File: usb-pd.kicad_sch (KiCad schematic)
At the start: 66 parts, among them J3 USB-C_GCT_USB4105-GF-A, Q4 BSS138-7-F, Q6 SQS401EN-T1_BE3, Q8 BSS138-7-F, Q9 BSS138-7-F, U5 CYPD3177-24LQXQ, U9 SIC477ED-T1-GE3

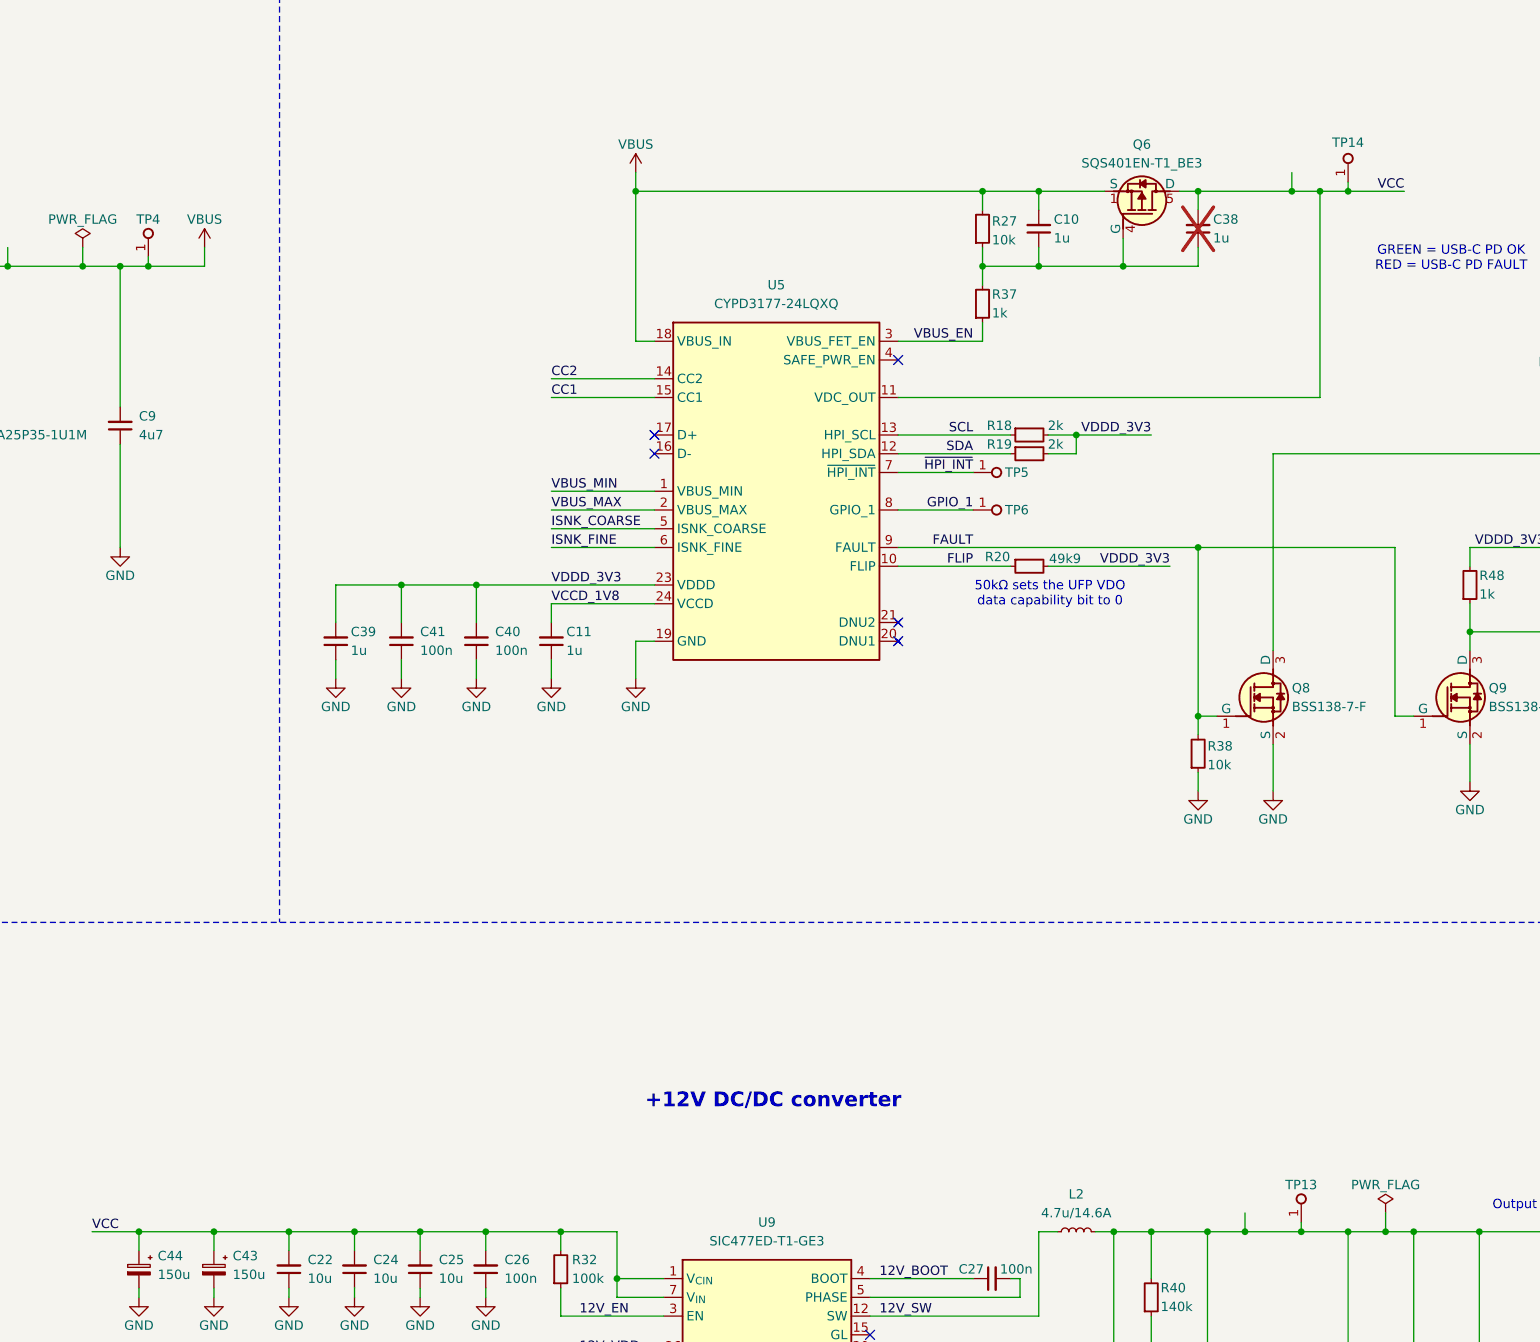
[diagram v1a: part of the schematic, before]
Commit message: [#79790] Added fiducials and double sided test points
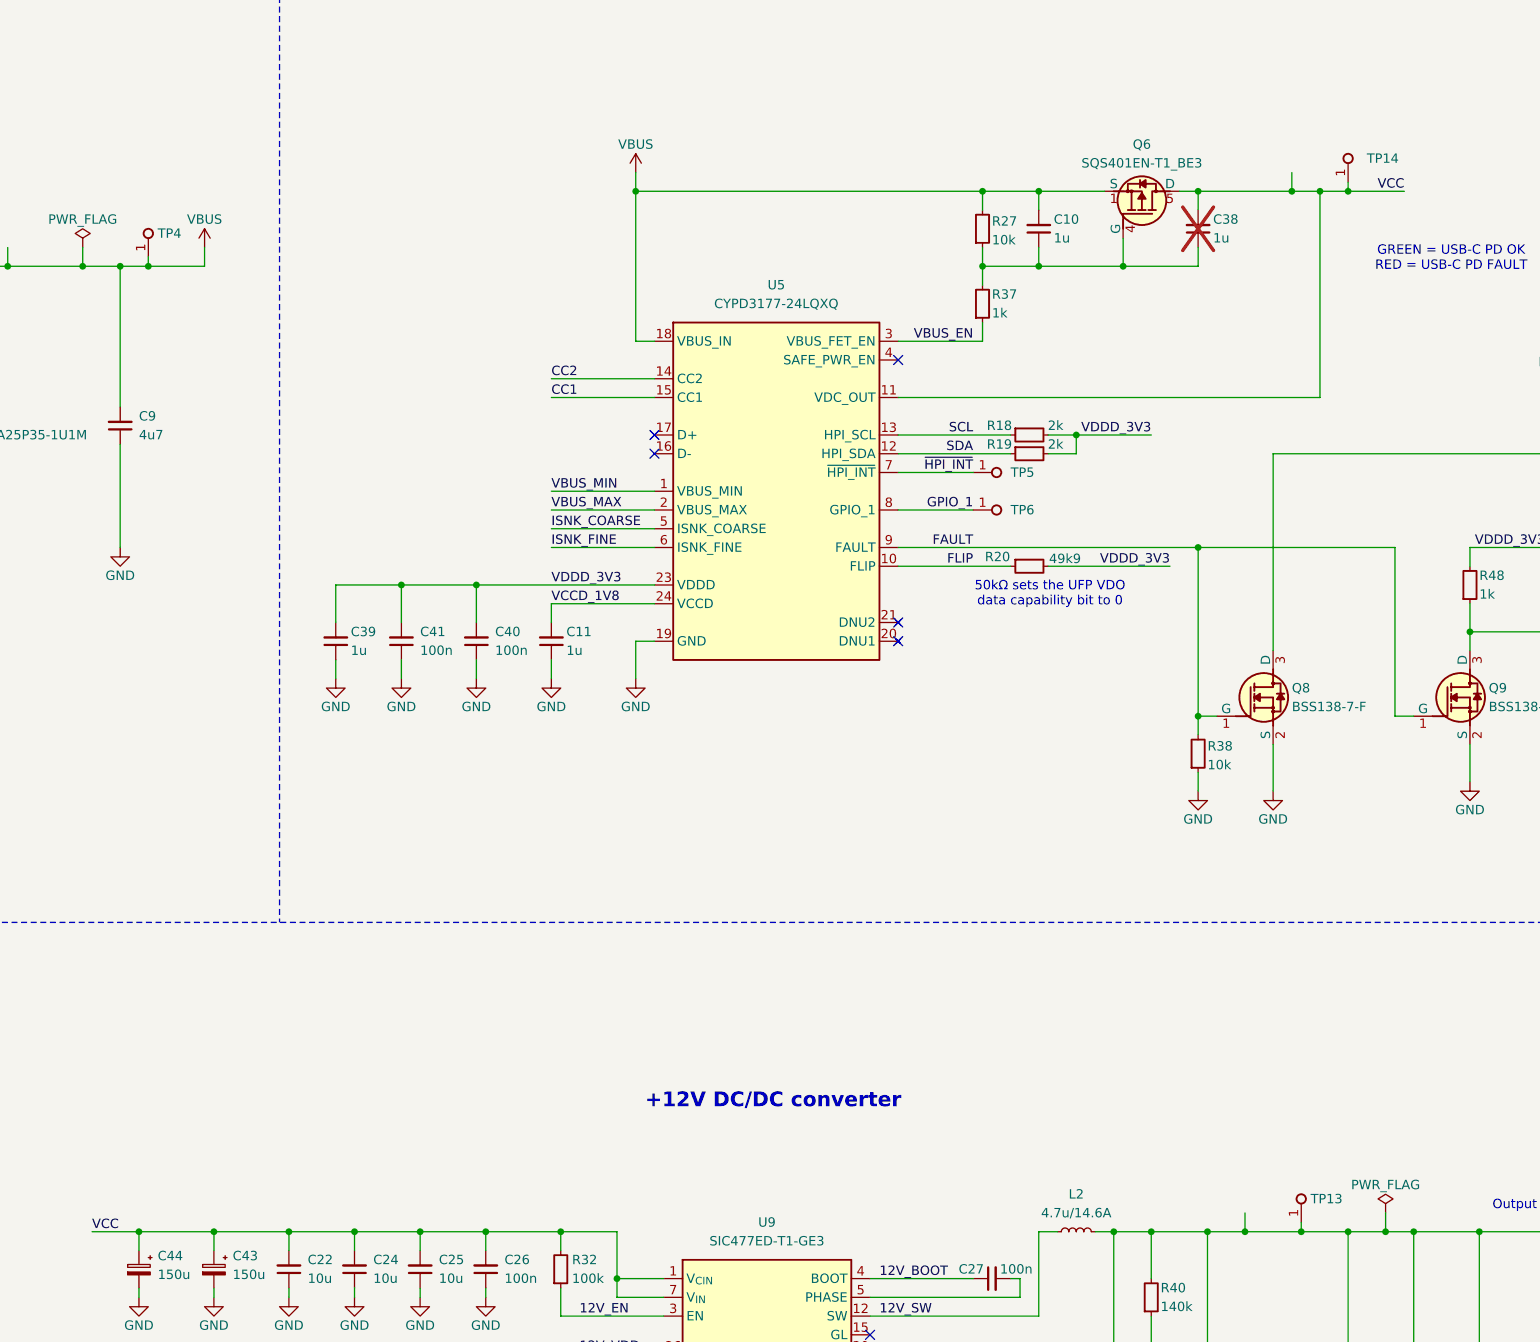
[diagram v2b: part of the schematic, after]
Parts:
- TP13, TP14, TP4, TP5, TP6: value TP_0.75mm_SMD -> TP_Pad0.75mm_Drill0.2mm; footprint antmicro-footprints:TP_SMD_0.75mm -> antmicro-footprints:TP_Pad0.75mm_Drill0.2mm; symbol antmicroTestPoints:TP_0.75mm_SMD -> antmicroTestPoints:TP_Pad0.75mm_Drill0.2mm
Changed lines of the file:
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@@
 	)
 	(table
-		(column_count 1)
-		(border
-			(external yes)
-			(header yes)
-			(stroke
-				(width 0)
-				(type solid)
-			)
-		)
-		(separators
-			(rows yes)
-			(cols yes)
-			(stroke
-				(width 0)
-				(type solid)
-			)
-		)
-		(column_widths 69.85)
-		(row_heights 3.81)
-		(cells
-			(table_cell "CONFIGURATION"
-				(exclude_from_sim no)
-				(at 330.2 26.67 0)
-				(size 69.85 3.81)
-				(margins 0.9525 0.9525 0.9525 0.9525)
-				(span 1 1)
-				(fill
-					(type none)
-				)
-				(effects
-					(font
-						(size 1.27 1.27)
-					)
-					(justify left top)
-				)
-			)
-		)
-	)
-	(table
 		(column_count 2)
 		(border
@@
 		)
 	)
+	(table
+		(column_count 1)
+		(border
+			(external yes)
+			(header yes)
+			(stroke
+				(width 0)
+				(type solid)
+			)
+		)
+		(separators
+			(rows yes)
+			(cols yes)
+			(stroke
+				(width 0)
+				(type solid)
+			)
+		)
+		(column_widths 69.85)
+		(row_heights 3.81)
+		(cells
+			(table_cell "CONFIGURATION"
+				(exclude_from_sim no)
+				(at 330.2 26.67 0)
+				(size 69.85 3.81)
+				(margins 0.9525 0.9525 0.9525 0.9525)
+				(span 1 1)
+				(fill
+					(type none)
+				)
+				(effects
+					(font
+						(size 1.27 1.27)
+					)
+					(justify left top)
+				)
+			)
+		)
+	)
 	(label "VDDD_3V3"
 		(at 332.74 50.8 0)
@@
 	)
 	(symbol
-		(lib_id "antmicroTestPoints:TP_0.75mm_SMD")
+		(lib_id "antmicroTestPoints:TP_Pad0.75mm_Drill0.2mm")
 		(at 218.44 96.52 0)
 		(unit 1)
@@
 		(on_board yes)
 		(dnp no)
+		(fields_autoplaced yes)
 		(property "Reference" "TP6"
-			(at 222.758 96.52 0)
+			(at 223.52 96.52 0)
 			(effects
 				(font
@@
 			)
 		)
-		(property "Value" "TP_0.75mm_SMD"
-			(at 229.235 100.33 0)
+		(property "Value" "TP_Pad0.75mm_Drill0.2mm"
+			(at 228.6 100.33 0)
 			(effects
 				(font
@@
 			)
 		)
-		(property "Footprint" "antmicro-footprints:TP_SMD_0.75mm"
-			(at 229.235 102.87 0)
+		(property "Footprint" "antmicro-footprints:TP_Pad0.75mm_Drill0.2mm"
+			(at 228.6 102.87 0)
 			(effects
 				(font
@@
 		)
 		(property "Author" "Antmicro"
-			(at 229.235 105.41 0)
+			(at 228.6 105.41 0)
 			(effects
 				(font
@@
 		)
 		(property "License" "Apache-2.0"
-			(at 229.235 107.95 0)
+			(at 228.6 107.95 0)
 			(effects
 				(font
@@
 	)
 	(symbol
-		(lib_id "antmicroTestPoints:TP_0.75mm_SMD")
+		(lib_id "antmicroTestPoints:TP_Pad0.75mm_Drill0.2mm")
 		(at 262.89 193.04 90)
 		(unit 1)
@@
 		(dnp no)
 		(property "Reference" "TP13"
-			(at 262.89 187.96 90)
+			(at 264.16 189.865 90)
 			(effects
 				(font
@@
 					(thickness 0.15)
 				)
+				(justify right)
 			)
 		)
-		(property "Value" "TP_0.75mm_SMD"
-			(at 266.7 182.245 0)
+		(property "Value" "TP_Pad0.75mm_Drill0.2mm"
+			(at 266.7 182.88 0)
 			(effects
 				(font
@@
 			)
 		)
-		(property "Footprint" "antmicro-footprints:TP_SMD_0.75mm"
-			(at 269.24 182.245 0)
+		(property "Footprint" "antmicro-footprints:TP_Pad0.75mm_Drill0.2mm"
+			(at 269.24 182.88 0)
 			(effects
 				(font
@@
 		)
 		(property "Author" "Antmicro"
-			(at 271.78 182.245 0)
+			(at 271.78 182.88 0)
 			(effects
 				(font
@@
 		)
 		(property "License" "Apache-2.0"
-			(at 274.32 182.245 0)
+			(at 274.32 182.88 0)
 			(effects
 				(font
@@
 	)
 	(symbol
-		(lib_id "antmicroTestPoints:TP_0.75mm_SMD")
+		(lib_id "antmicroTestPoints:TP_Pad0.75mm_Drill0.2mm")
 		(at 269.24 52.07 90)
 		(unit 1)
@@
 		(on_board yes)
 		(dnp no)
+		(fields_autoplaced yes)
 		(property "Reference" "TP14"
-			(at 269.24 46.736 90)
+			(at 271.78 48.895 90)
 			(effects
 				(font
@@
 					(thickness 0.15)
 				)
+				(justify right)
 			)
 		)
-		(property "Value" "TP_0.75mm_SMD"
-			(at 273.05 41.275 0)
+		(property "Value" "TP_Pad0.75mm_Drill0.2mm"
+			(at 273.05 41.91 0)
 			(effects
 				(font
@@
 			)
 		)
-		(property "Footprint" "antmicro-footprints:TP_SMD_0.75mm"
-			(at 275.59 41.275 0)
+		(property "Footprint" "antmicro-footprints:TP_Pad0.75mm_Drill0.2mm"
+			(at 275.59 41.91 0)
 			(effects
 				(font
@@
 		)
 		(property "Author" "Antmicro"
-			(at 278.13 41.275 0)
+			(at 278.13 41.91 0)
 			(effects
 				(font
@@
 		)
 		(property "License" "Apache-2.0"
-			(at 280.67 41.275 0)
+			(at 280.67 41.91 0)
 			(effects
 				(font
@@
 	)
 	(symbol
-		(lib_id "antmicroTestPoints:TP_0.75mm_SMD")
+		(lib_id "antmicroTestPoints:TP_Pad0.75mm_Drill0.2mm")
 		(at 218.44 91.44 0)
 		(unit 1)
@@
 		(on_board yes)
 		(dnp no)
+		(fields_autoplaced yes)
 		(property "Reference" "TP5"
-			(at 222.758 91.44 0)
+			(at 223.52 91.44 0)
 			(effects
 				(font
@@
 			)
 		)
-		(property "Value" "TP_0.75mm_SMD"
-			(at 229.235 95.25 0)
+		(property "Value" "TP_Pad0.75mm_Drill0.2mm"
+			(at 228.6 95.25 0)
 			(effects
 				(font
@@
 			)
 		)
-		(property "Footprint" "antmicro-footprints:TP_SMD_0.75mm"
-			(at 229.235 97.79 0)
+		(property "Footprint" "antmicro-footprints:TP_Pad0.75mm_Drill0.2mm"
+			(at 228.6 97.79 0)
 			(effects
 				(font
@@
 		)
 		(property "Author" "Antmicro"
-			(at 229.235 100.33 0)
+			(at 228.6 100.33 0)
 			(effects
 				(font
@@
 		)
 		(property "License" "Apache-2.0"
-			(at 229.235 102.87 0)
+			(at 228.6 102.87 0)
 			(effects
 				(font
@@
 	)
 	(symbol
-		(lib_id "antmicroTestPoints:TP_0.75mm_SMD")
+		(lib_id "antmicroTestPoints:TP_Pad0.75mm_Drill0.2mm")
 		(at 106.68 62.23 90)
 		(unit 1)
@@
 		(dnp no)
 		(property "Reference" "TP4"
-			(at 106.68 57.15 90)
+			(at 107.95 59.055 90)
 			(effects
 				(font
@@
 					(thickness 0.15)
 				)
+				(justify right)
 			)
 		)
-		(property "Value" "TP_0.75mm_SMD"
-			(at 110.49 51.435 0)
+		(property "Value" "TP_Pad0.75mm_Drill0.2mm"
+			(at 110.49 52.07 0)
 			(effects
 				(font
@@
 			)
 		)
-		(property "Footprint" "antmicro-footprints:TP_SMD_0.75mm"
-			(at 113.03 51.435 0)
+		(property "Footprint" "antmicro-footprints:TP_Pad0.75mm_Drill0.2mm"
+			(at 113.03 52.07 0)
 			(effects
 				(font
@@
 		)
 		(property "Author" "Antmicro"
-			(at 115.57 51.435 0)
+			(at 115.57 52.07 0)
 			(effects
 				(font
@@
 		)
 		(property "License" "Apache-2.0"
-			(at 118.11 51.435 0)
+			(at 118.11 52.07 0)
 			(effects
 				(font
